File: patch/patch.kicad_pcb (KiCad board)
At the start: 4 copper layers, 20 x 108 mm, 22 parts, among them J1 Eurorack_Power, J2 Eurorack_Mono_Jack, J3 Eurorack_Mono_Jack, J4 Eurorack_Mono_Jack_No_S, J5 Eurorack_Mono_Jack_No_S, U1 OPA4991

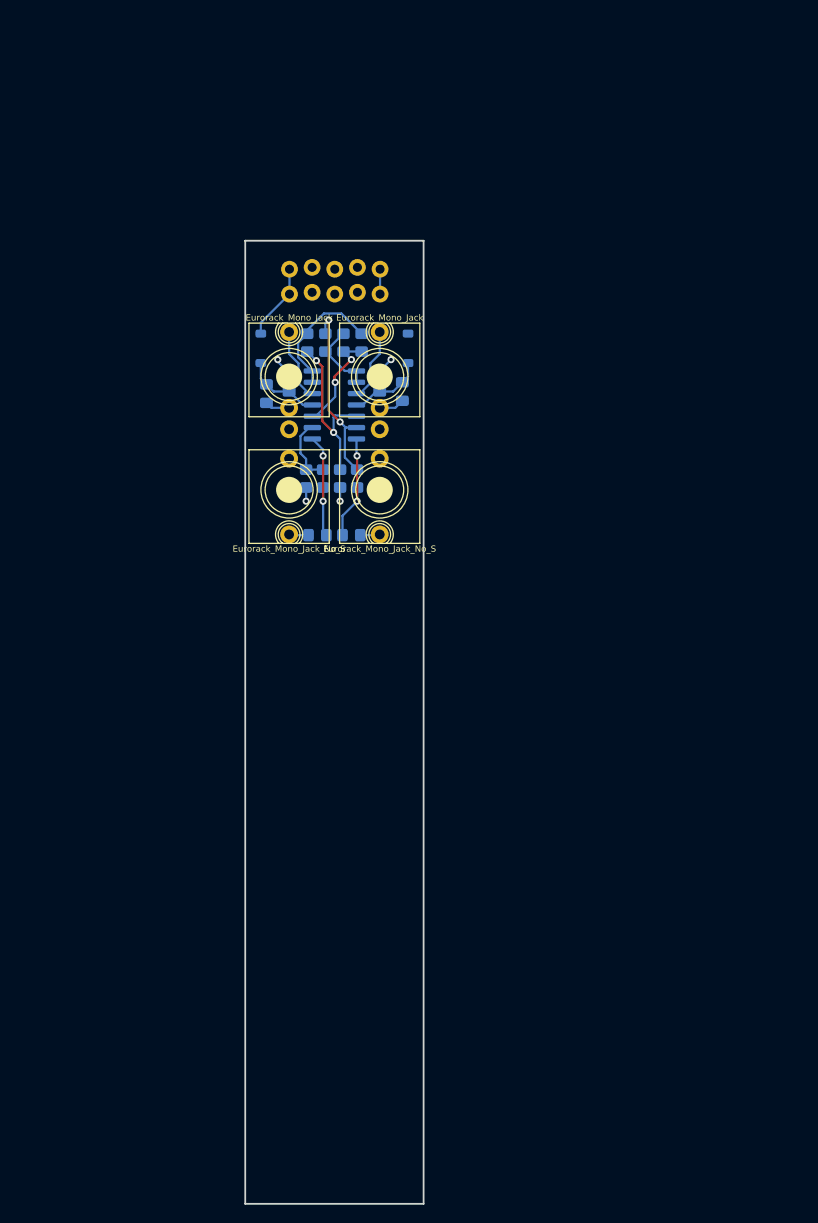
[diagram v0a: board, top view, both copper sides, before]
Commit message: Patch: Start of feedback, more channels
Addressed some feedback, switched to TSSOP/0603 to get better margins.
Started on more channels to make sure the jack and part placement is OK.
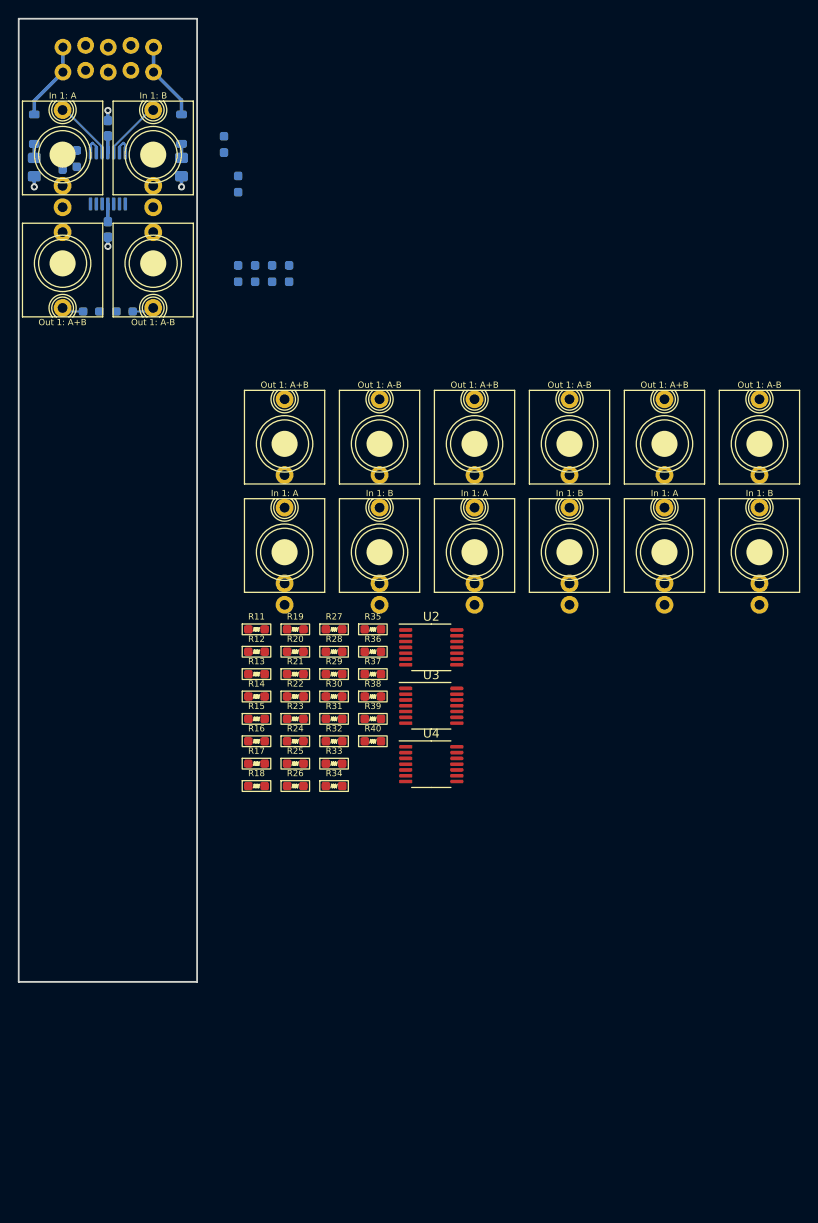
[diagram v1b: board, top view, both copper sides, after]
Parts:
- added J10: In 1: A, winterbloom:AudioJack_WQP518MA_Compact_S, F.Cu at (41.1, 60.3)
- added J11: In 1: B, winterbloom:AudioJack_WQP518MA_Compact_S, F.Cu at (51.8, 60.3)
- added J12: Out 1: A+B, winterbloom:AudioJack_WQP518MA_No_S, F.Cu at (41.1, 48.2)
- added J13: Out 1: A-B, winterbloom:AudioJack_WQP518MA_No_S, F.Cu at (51.8, 48.2)
- added J14: In 1: A, winterbloom:AudioJack_WQP518MA_Compact_S, F.Cu at (62.4, 60.3)
- added J15: In 1: B, winterbloom:AudioJack_WQP518MA_Compact_S, F.Cu at (73.1, 60.3)
- added J16: Out 1: A+B, winterbloom:AudioJack_WQP518MA_No_S, F.Cu at (62.4, 48.2)
- added J17: Out 1: A-B, winterbloom:AudioJack_WQP518MA_No_S, F.Cu at (73.1, 48.2)
- added J6: In 1: A, winterbloom:AudioJack_WQP518MA_Compact_S, F.Cu at (19.8, 60.3)
- added J7: In 1: B, winterbloom:AudioJack_WQP518MA_Compact_S, F.Cu at (30.5, 60.3)
- added J8: Out 1: A+B, winterbloom:AudioJack_WQP518MA_No_S, F.Cu at (19.8, 48.2)
- added J9: Out 1: A-B, winterbloom:AudioJack_WQP518MA_No_S, F.Cu at (30.5, 48.2)
- added R11: 10k, winterbloom:R_0603_HandSolder, F.Cu at (16.7, 69.0)
- added R12: 10k, winterbloom:R_0603_HandSolder, F.Cu at (16.7, 71.5)
- added R13: 10k, winterbloom:R_0603_HandSolder, F.Cu at (16.7, 74.0)
- added R14: 10k, winterbloom:R_0603_HandSolder, F.Cu at (16.7, 76.5)
- added R15: 51R, winterbloom:R_0603_HandSolder, F.Cu at (16.7, 79.0)
- added R16: 51R, winterbloom:R_0603_HandSolder, F.Cu at (16.7, 81.5)
- added R17: 10k, winterbloom:R_0603_HandSolder, F.Cu at (16.7, 84.0)
- added R18: 10k, winterbloom:R_0603_HandSolder, F.Cu at (16.7, 86.5)
- added R19: 10k, winterbloom:R_0603_HandSolder, F.Cu at (21.0, 69.0)
- added R20: 10k, winterbloom:R_0603_HandSolder, F.Cu at (21.0, 71.5)
- added R21: 10k, winterbloom:R_0603_HandSolder, F.Cu at (21.0, 74.0)
- added R22: 10k, winterbloom:R_0603_HandSolder, F.Cu at (21.0, 76.5)
- added R23: 10k, winterbloom:R_0603_HandSolder, F.Cu at (21.0, 79.0)
- added R24: 10k, winterbloom:R_0603_HandSolder, F.Cu at (21.0, 81.5)
- added R25: 51R, winterbloom:R_0603_HandSolder, F.Cu at (21.0, 84.0)
- added R26: 51R, winterbloom:R_0603_HandSolder, F.Cu at (21.0, 86.5)
- added R27: 10k, winterbloom:R_0603_HandSolder, F.Cu at (25.4, 69.0)
- added R28: 10k, winterbloom:R_0603_HandSolder, F.Cu at (25.4, 71.5)
- added R29: 10k, winterbloom:R_0603_HandSolder, F.Cu at (25.4, 74.0)
- added R30: 10k, winterbloom:R_0603_HandSolder, F.Cu at (25.4, 76.5)
- added R31: 10k, winterbloom:R_0603_HandSolder, F.Cu at (25.4, 79.0)
- added R32: 10k, winterbloom:R_0603_HandSolder, F.Cu at (25.4, 81.5)
- added R33: 10k, winterbloom:R_0603_HandSolder, F.Cu at (25.4, 84.0)
- added R34: 10k, winterbloom:R_0603_HandSolder, F.Cu at (25.4, 86.5)
- added R35: 51R, winterbloom:R_0603_HandSolder, F.Cu at (29.7, 69.0)
- added R36: 51R, winterbloom:R_0603_HandSolder, F.Cu at (29.7, 71.5)
- added R37: 10k, winterbloom:R_0603_HandSolder, F.Cu at (29.7, 74.0)
- added R38: 10k, winterbloom:R_0603_HandSolder, F.Cu at (29.7, 76.5)
- added R39: 10k, winterbloom:R_0603_HandSolder, F.Cu at (29.7, 79.0)
- added R40: 10k, winterbloom:R_0603_HandSolder, F.Cu at (29.7, 81.5)
- added U2: OPA4991, Package_SO:TSSOP-14_4.4x5mm_P0.65mm, F.Cu at (36.3, 71.0)
- added U3: OPA4991, Package_SO:TSSOP-14_4.4x5mm_P0.65mm, F.Cu at (36.3, 77.5)
- added U4: OPA4991, Package_SO:TSSOP-14_4.4x5mm_P0.65mm, F.Cu at (36.3, 84.1)
- C1, C3: value 10uF -> 10u; footprint Capacitor_SMD:C_0805_2012Metric_Pad1.18x1.45mm_HandSolder -> winterbloom:C_0805_HandSolder
- C2, C4: value 100nF -> 100n; footprint Capacitor_SMD:C_0805_2012Metric_Pad1.18x1.45mm_HandSolder -> winterbloom:C_0603_HandSolder
- D1, D2: value D_Schottky -> 30V
- J2: value Eurorack_Mono_Jack -> In 1: A
- J3: value Eurorack_Mono_Jack -> In 1: B
- J4: value Eurorack_Mono_Jack_No_S -> Out 1: A+B
- J5: value Eurorack_Mono_Jack_No_S -> Out 1: A-B
- R1, R10, R2, R3, R4, R7, R8, R9: footprint Resistor_SMD:R_0805_2012Metric_Pad1.20x1.40mm_HandSolder -> winterbloom:R_0603_HandSolder
- R5, R6: value 51 -> 51R; footprint Resistor_SMD:R_0805_2012Metric_Pad1.20x1.40mm_HandSolder -> winterbloom:R_0603_HandSolder
- U1: footprint Package_SO:SOIC-14_3.9x8.7mm_P1.27mm -> Package_SO:TSSOP-14_4.4x5mm_P0.65mm
- moved R1 39.2 mm to (-5.08, 16.5)
- moved C1 36.4 mm to (-8.26, 17.1)
- moved R2 36.3 mm to (-3.49, 16.2)
- moved J4 35.9 mm to (-5.08, 27.9)
- moved J5 35.9 mm to (5.08, 27.9)
- moved U1 35.9 mm to (0.00, 18.4), turned to -90 degrees
- moved R6 35.7 mm to (1.86, 33.3)
- moved R5 35.7 mm to (-1.86, 33.3)
- moved J2 35.6 mm to (-5.08, 15.7)
- moved J3 35.6 mm to (5.08, 15.7)
- moved J1 35.6 mm to (5.12, 6.40)
- moved D1 35.3 mm to (-8.26, 12.9)
- moved D2 35.3 mm to (8.26, 12.9)
- moved C3 35.3 mm to (8.26, 17.1)
- moved C2 35.0 mm to (0.00, 12.8)
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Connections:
- R1 pad 1: Net-(U1A-+) -> Net-(U1D-+)
- R1 pad 2: Net-(U1B--) -> Net-(U1A--)
- R10 pad 2: Net-(U1A--) -> Net-(U1D--)
- R2 pad 1: Net-(U1C--) -> Net-(U1B--)
- R2 pad 2: Net-(U1A-+) -> Net-(U1D-+)
- R3 pad 1: Net-(U1D--) -> Net-(U1C--)
- R3 pad 2: Net-(U1C--) -> Net-(U1B--)
- R4 pad 1: Net-(U1D-+) -> Net-(U1C-+)
- R4 pad 2: Net-(U1B--) -> Net-(U1A--)
- R7 pad 1: Net-(U1A--) -> Net-(U1D--)
- R8 pad 2: Net-(U1D-+) -> Net-(U1C-+)
- R9 pad 1: Net-(U1D--) -> Net-(U1C--)
- U1 pad 1: Net-(R5-Pad1) -> Net-(U1A--)
- U1 pad 10: Net-(J3-Tip) -> Net-(U1C-+)
- U1 pad 14: Net-(R6-Pad1) -> Net-(R5-Pad1)
- U1 pad 3: Net-(U1A-+) -> Net-(J2-Tip)
- U1 pad 5: Net-(J2-Tip) -> Net-(J3-Tip)
- U1 pad 8: Net-(U1C--) -> Net-(R6-Pad1)
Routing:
- net Net-(U1D--): track 21.1 -> 0.00 mm, vias 2 -> 0
- net Net-(U1D-+): track 19.0 -> 0.00 mm, vias 2 -> 0
- net Net-(R6-Pad1): track 13.0 -> 0.00 mm, vias 2 -> 0
- net Net-(R5-Pad1): track 12.5 -> 0.00 mm, vias 2 -> 0
- net Net-(U1B--): track 14.3 -> 2.52 mm
- net Net-(U1A-+): track 11.4 -> 0.00 mm, vias 2 -> 0
- net Net-(U1C--): track 8.49 -> 0.00 mm
- net GND: track 12.5 -> 4.14 mm
- net Net-(D2-K): track 2.79 -> 8.52 mm
- net VCC: track 8.71 -> 3.47 mm
- net Net-(U1A--): track 7.28 -> 2.52 mm
- net VEE: track 8.09 -> 3.56 mm
- net Net-(J3-Tip): track 7.83 -> 6.82 mm
- net Net-(J2-Tip): track 7.83 -> 6.82 mm
